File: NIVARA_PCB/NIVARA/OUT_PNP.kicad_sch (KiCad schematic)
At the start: 0 parts

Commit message: ACTUALIZACION DE SALIDAS NPN Y PNP
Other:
- added sheet O_PNP (O_PNP.kicad_sch)
- added sheet O_PNP1 (O_PNP.kicad_sch)
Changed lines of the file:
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@@
 	(generator_version "9.0")
 	(paper "A4")
+	(wire
+		(pts
+			(xy 48.26 58.42) (xy 52.07 58.42)
+		)
+		(stroke
+			(width 0)
+			(type default)
+		)
+	)
+	(wire
+		(pts
+			(xy 44.45 87.63) (xy 52.07 87.63)
+		)
+		(stroke
+			(width 0)
+			(type default)
+		)
+	)
+	(wire
+		(pts
+			(xy 81.28 58.42) (xy 85.09 58.42)
+		)
+		(stroke
+			(width 0)
+			(type default)
+		)
+	)
+	(wire
+		(pts
+			(xy 81.28 87.63) (xy 87.63 87.63)
+		)
+		(stroke
+			(width 0)
+			(type default)
+		)
+	)
+	(hierarchical_label "OUT_2"
+		(shape output)
+		(at 87.63 87.63 0)
+		(effects
+			(font
+				(size 1.27 1.27)
+			)
+			(justify left)
+		)
+	)
 	(hierarchical_label "IN_1"
 		(shape input)
-		(at 170.18 57.15 180)
+		(at 48.26 58.42 180)
 		(effects
 			(font
@@
 		)
 	)
-	(hierarchical_label "OUT_2"
-		(shape output)
-		(at 191.77 64.77 0)
-		(effects
-			(font
-				(size 1.27 1.27)
-			)
-			(justify left)
-		)
-	)
 	(hierarchical_label "OUT_1"
 		(shape output)
-		(at 191.77 57.15 0)
+		(at 85.09 58.42 0)
 		(effects
 			(font
@@
 	(hierarchical_label "IN_2"
 		(shape input)
-		(at 170.18 64.77 180)
+		(at 44.45 87.63 180)
 		(effects
 			(font
@@
 		)
 	)
+	(sheet
+		(at 52.07 80.01)
+		(size 29.21 16.51)
+		(exclude_from_sim no)
+		(in_bom yes)
+		(on_board yes)
+		(dnp no)
+		(fields_autoplaced yes)
+		(stroke
+			(width 0.1524)
+			(type solid)
+		)
+		(fill
+			(color 0 0 0 0.0000)
+		)
+		(property "Sheetname" "O_PNP1"
+			(at 52.07 79.2984 0)
+			(effects
+				(font
+					(size 1.27 1.27)
+				)
+				(justify left bottom)
+			)
+		)
+		(property "Sheetfile" "O_PNP.kicad_sch"
+			(at 52.07 97.1046 0)
+			(effects
+				(font
+					(size 1.27 1.27)
+				)
+				(justify left top)
+			)
+		)
+		(pin "OUT" input
+			(at 81.28 87.63 0)
+			(effects
+				(font
+					(size 1.27 1.27)
+				)
+				(justify right)
+			)
+		)
+		(pin "IN" input
+			(at 52.07 87.63 180)
+			(effects
+				(font
+					(size 1.27 1.27)
+				)
+				(justify left)
+			)
+		)
+		(instances
+			(project "NIVARA"
+				(path "/6298d7d5-28da-40bf-9586-24a8e5c02b82/7ff0dada-fc46-483c-91ad-b264be8c64cf/83581511-a4ee-4ab3-83b5-847131b17a04"
+					(page "28")
+				)
+			)
+		)
+	)
+	(sheet
+		(at 52.07 50.8)
+		(size 29.21 16.51)
+		(exclude_from_sim no)
+		(in_bom yes)
+		(on_board yes)
+		(dnp no)
+		(fields_autoplaced yes)
+		(stroke
+			(width 0.1524)
+			(type solid)
+		)
+		(fill
+			(color 0 0 0 0.0000)
+		)
+		(property "Sheetname" "O_PNP"
+			(at 52.07 50.0884 0)
+			(effects
+				(font
+					(size 1.27 1.27)
+				)
+				(justify left bottom)
+			)
+		)
+		(property "Sheetfile" "O_PNP.kicad_sch"
+			(at 52.07 67.8946 0)
+			(effects
+				(font
+					(size 1.27 1.27)
+				)
+				(justify left top)
+			)
+		)
+		(pin "OUT" input
+			(at 81.28 58.42 0)
+			(effects
+				(font
+					(size 1.27 1.27)
+				)
+				(justify right)
+			)
+		)
+		(pin "IN" input
+			(at 52.07 58.42 180)
+			(effects
+				(font
+					(size 1.27 1.27)
+				)
+				(justify left)
+			)
+		)
+		(instances
+			(project "NIVARA"
+				(path "/6298d7d5-28da-40bf-9586-24a8e5c02b82/7ff0dada-fc46-483c-91ad-b264be8c64cf/83581511-a4ee-4ab3-83b5-847131b17a04"
+					(page "27")
+				)
+			)
+		)
+	)

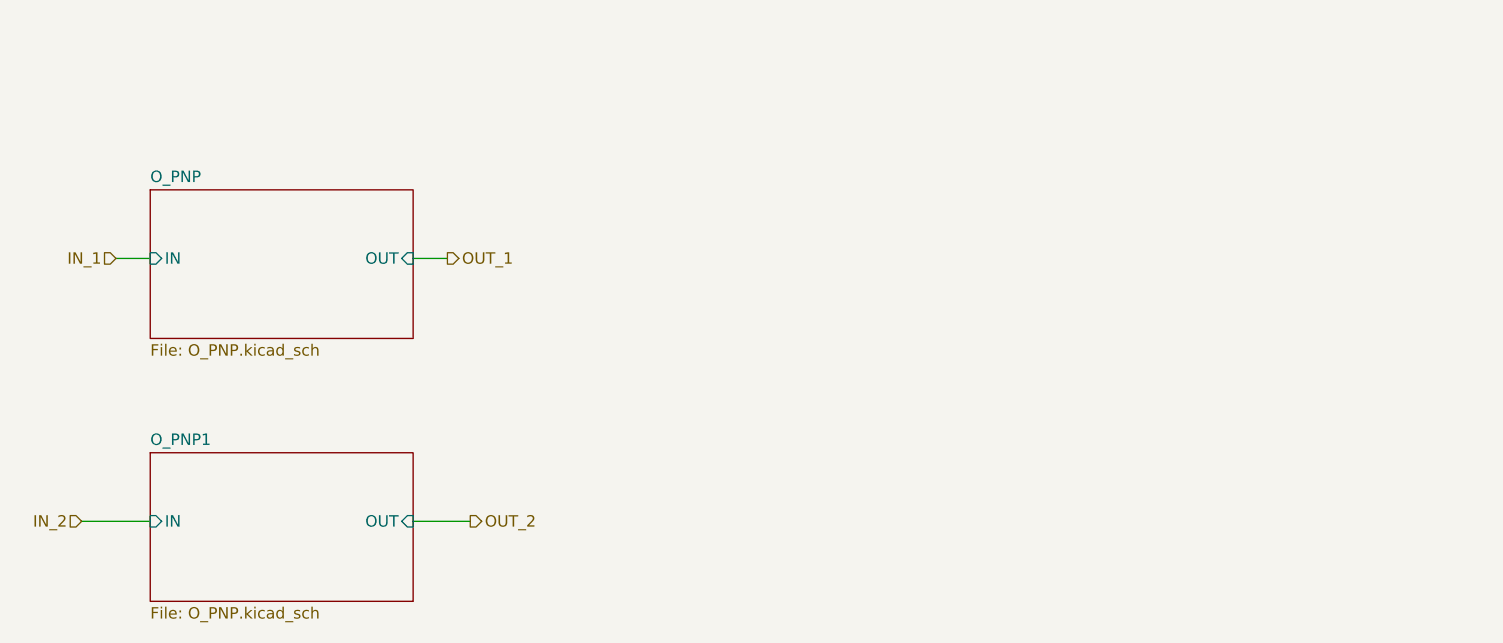
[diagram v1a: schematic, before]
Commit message: arreglo del desastre que tenia con las salidas PNP
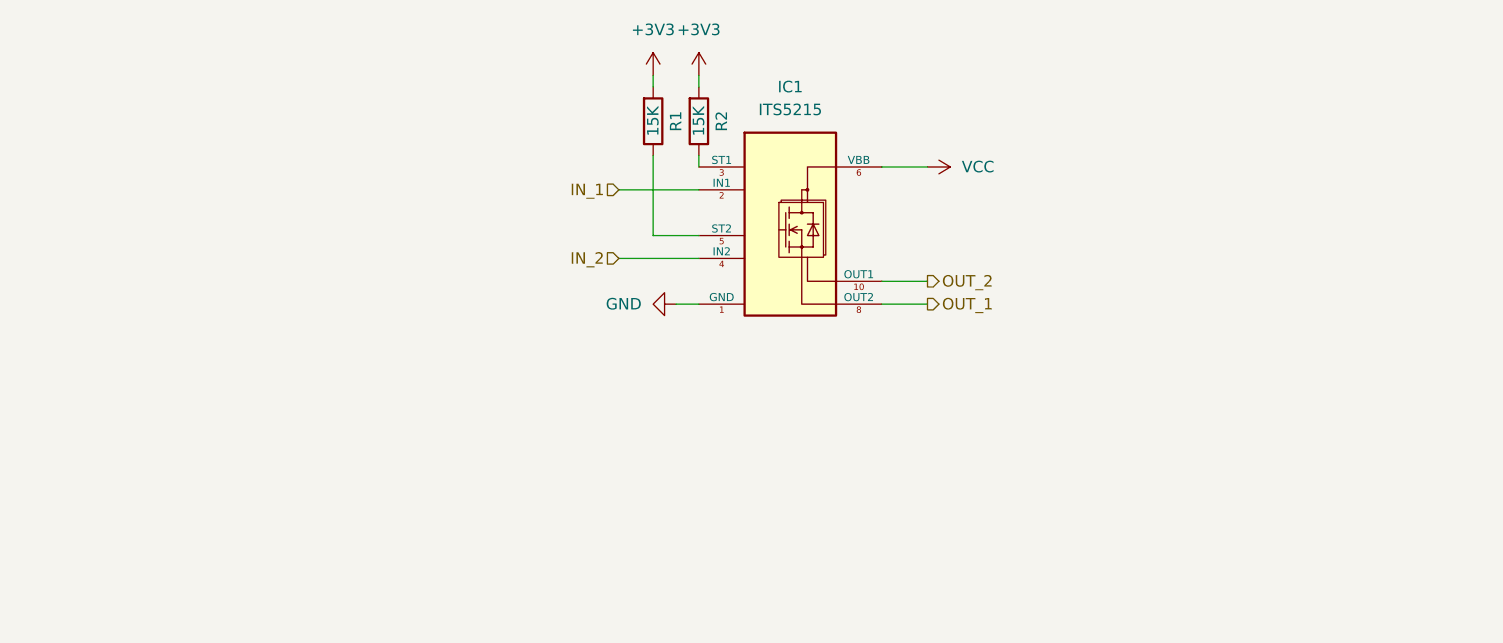
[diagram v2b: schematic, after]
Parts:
- added IC1: ITS5215, Package_SO:Infineon_PG-DSO-12-9_ThermalVias, symbol Power_Management:ITS5215
- added R1, R2: 15K, PCM_Resistor_SMD_AKL:R_0603_1608Metric, symbol PCM_Resistor_AKL:R_0603
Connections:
- net IN_1: now also IC1.2 (IN1)
- net IN_2: now also IC1.4 (IN2)
- net OUT_1: now also IC1.8 (OUT2)
- net OUT_2: now also IC1.10 (OUT1)
- new net: IC1.5 (ST2), R1.2
- new net: IC1.3 (ST1), R2.2
- new net +3V3: R1.1, R2.1
- new net GND: IC1.1 (GND)
- new net VCC: IC1.12 (VBB), IC1.13 (VBB), IC1.6 (VBB)
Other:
- removed sheet O_PNP
- removed sheet O_PNP1
